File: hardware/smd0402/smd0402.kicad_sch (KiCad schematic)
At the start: 33 parts, among them J1 Conn_01x04, J2 Conn_01x03, U1 WCH CH32V003F4U6

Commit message: tweak toward JLC assembly files
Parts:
- C1, D1, R1: JLC (none) -> 0402

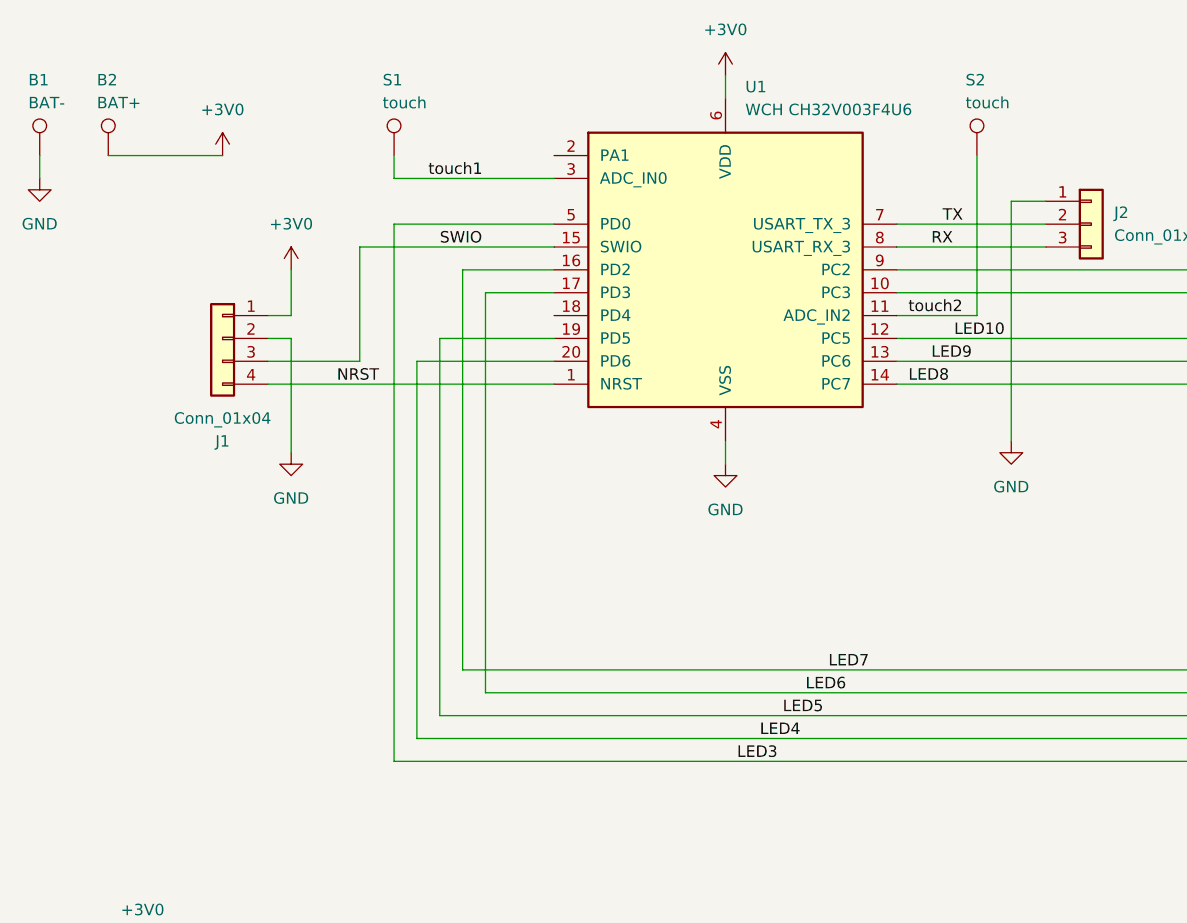
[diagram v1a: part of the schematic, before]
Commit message: reassign touch pads to OPNx
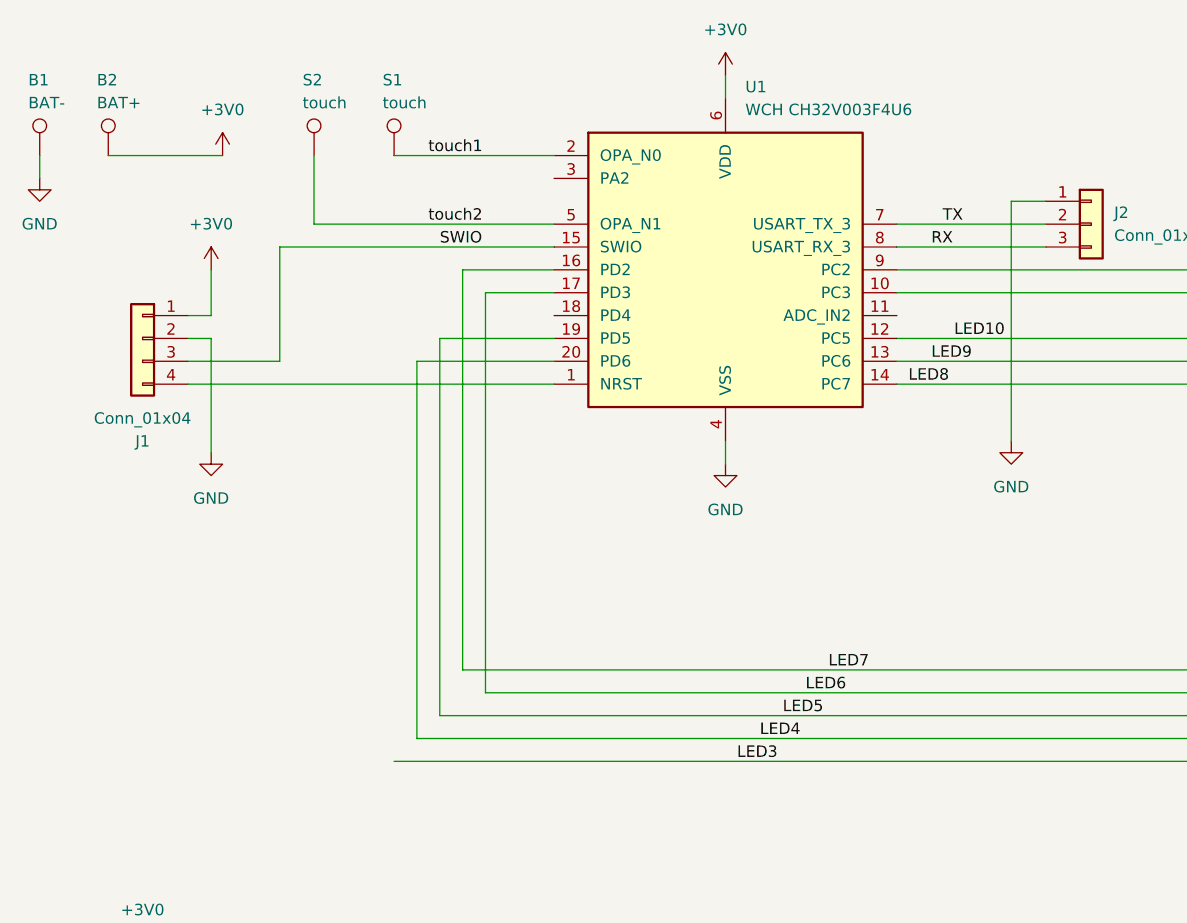
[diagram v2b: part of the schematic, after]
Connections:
- net LED3: no longer U1.5 (PD0)
- net touch1: now also U1.2 (PA1); no longer U1.3 (PA2)
- net touch2: now also U1.5 (PD0); no longer U1.11 (PC4)
- net NRST: no longer names the net of J1.4 (Pin_4), U1.1 (PD7)
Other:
- moved on the sheet: J1, S2
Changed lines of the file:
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@@
 	(wire
 		(pts
+			(xy 88.9 57.15) (xy 62.23 57.15)
+		)
+		(stroke
+			(width 0)
+			(type default)
+		)
+	)
+	(wire
+		(pts
 			(xy 176.53 62.23) (xy 127 62.23)
 		)
@@
 	(wire
 		(pts
-			(xy 57.15 69.85) (xy 59.69 69.85)
+			(xy 48.26 69.85) (xy 50.8 69.85)
 		)
 		(stroke
@@
 	(wire
 		(pts
-			(xy 67.31 59.69) (xy 88.9 59.69)
+			(xy 58.42 59.69) (xy 88.9 59.69)
 		)
 		(stroke
@@
 	(wire
 		(pts
-			(xy 59.69 67.31) (xy 57.15 67.31)
+			(xy 50.8 67.31) (xy 48.26 67.31)
 		)
 		(stroke
@@
 	(wire
 		(pts
-			(xy 57.15 74.93) (xy 88.9 74.93)
-		)
-		(stroke
-			(width 0)
-			(type default)
-		)
-	)
-	(wire
-		(pts
-			(xy 71.12 57.15) (xy 71.12 116.84)
-		)
-		(stroke
-			(width 0)
-			(type default)
-		)
-	)
-	(wire
-		(pts
 			(xy 217.17 161.29) (xy 228.6 161.29)
 		)
@@
 	(wire
 		(pts
-			(xy 71.12 52.07) (xy 71.12 49.53)
-		)
-		(stroke
-			(width 0)
-			(type default)
-		)
-	)
-	(wire
-		(pts
 			(xy 166.37 158.75) (xy 166.37 161.29)
 		)
@@
 	(wire
 		(pts
-			(xy 135.89 67.31) (xy 127 67.31)
+			(xy 107.95 149.86) (xy 121.92 149.86)
 		)
 		(stroke
@@
 	(wire
 		(pts
-			(xy 107.95 149.86) (xy 121.92 149.86)
+			(xy 238.76 148.59) (xy 238.76 151.13)
 		)
 		(stroke
@@
 	(wire
 		(pts
-			(xy 238.76 148.59) (xy 238.76 151.13)
+			(xy 62.23 57.15) (xy 62.23 49.53)
 		)
 		(stroke
@@
 	(wire
 		(pts
-			(xy 71.12 57.15) (xy 88.9 57.15)
+			(xy 52.07 149.86) (xy 67.31 149.86)
 		)
 		(stroke
@@
 	(wire
 		(pts
-			(xy 52.07 149.86) (xy 67.31 149.86)
+			(xy 31.75 49.53) (xy 31.75 52.07)
 		)
 		(stroke
@@
 	(wire
 		(pts
-			(xy 31.75 49.53) (xy 31.75 52.07)
+			(xy 88.9 49.53) (xy 71.12 49.53)
 		)
 		(stroke
@@
 	(wire
 		(pts
-			(xy 88.9 52.07) (xy 71.12 52.07)
+			(xy 166.37 140.97) (xy 166.37 64.77)
 		)
 		(stroke
@@
 	(wire
 		(pts
-			(xy 166.37 140.97) (xy 166.37 64.77)
+			(xy 43.18 138.43) (xy 43.18 142.24)
 		)
 		(stroke
@@
 	(wire
 		(pts
-			(xy 43.18 138.43) (xy 43.18 142.24)
+			(xy 50.8 62.23) (xy 50.8 67.31)
 		)
 		(stroke
@@
 	(wire
 		(pts
-			(xy 59.69 62.23) (xy 59.69 67.31)
+			(xy 48.26 74.93) (xy 88.9 74.93)
 		)
 		(stroke
@@
 	(wire
 		(pts
-			(xy 67.31 72.39) (xy 57.15 72.39)
+			(xy 58.42 72.39) (xy 48.26 72.39)
 		)
 		(stroke
@@
 	(wire
 		(pts
-			(xy 135.89 49.53) (xy 135.89 67.31)
-		)
-		(stroke
-			(width 0)
-			(type default)
-		)
-	)
-	(wire
-		(pts
 			(xy 207.01 161.29) (xy 217.17 161.29)
 		)
@@
 	(wire
 		(pts
-			(xy 59.69 69.85) (xy 59.69 82.55)
+			(xy 50.8 69.85) (xy 50.8 82.55)
 		)
 		(stroke
@@
 	(wire
 		(pts
-			(xy 67.31 59.69) (xy 67.31 72.39)
+			(xy 58.42 59.69) (xy 58.42 72.39)
 		)
 		(stroke
@@
 	(label "LED10"
 		(at 133.35 69.85 0)
-		(fields_autoplaced yes)
 		(effects
 			(font
@@
 	(label "LED4"
 		(at 111.76 114.3 0)
-		(fields_autoplaced yes)
 		(effects
 			(font
@@
 	(label "TX"
 		(at 132.08 57.15 0)
-		(fields_autoplaced yes)
 		(effects
 			(font
@@
 	(label "LED8"
 		(at 128.27 74.93 0)
-		(fields_autoplaced yes)
 		(effects
 			(font
@@
 	(label "LED9"
 		(at 130.81 72.39 0)
-		(fields_autoplaced yes)
 		(effects
 			(font
@@
 	(label "LED2"
 		(at 163.83 62.23 0)
-		(fields_autoplaced yes)
 		(effects
 			(font
@@
 	(label "LED7"
 		(at 119.38 106.68 0)
-		(fields_autoplaced yes)
-		(effects
-			(font
-				(size 1.27 1.27)
-			)
-			(justify left bottom)
-		)
-	)
-	(label "NRST"
-		(at 64.77 74.93 0)
-		(fields_autoplaced yes)
 		(effects
 			(font
@@
 	)
 	(label "touch1"
-		(at 74.93 52.07 0)
-		(fields_autoplaced yes)
+		(at 74.93 49.53 0)
 		(effects
 			(font
@@
 	)
 	(label "touch2"
-		(at 128.27 67.31 0)
-		(fields_autoplaced yes)
+		(at 74.93 57.15 0)
 		(effects
 			(font
@@
 	(label "LED1"
 		(at 161.29 64.77 0)
-		(fields_autoplaced yes)
 		(effects
 			(font
@@
 	(label "LED5"
 		(at 114.3 111.76 0)
-		(fields_autoplaced yes)
 		(effects
 			(font
@@
 	(label "SWIO"
 		(at 76.2 59.69 0)
-		(fields_autoplaced yes)
 		(effects
 			(font
@@
 	(label "RX"
 		(at 130.81 59.69 0)
-		(fields_autoplaced yes)
 		(effects
 			(font
@@
 	(label "LED3"
 		(at 109.22 116.84 0)
-		(fields_autoplaced yes)
 		(effects
 			(font
@@
 	(label "LED6"
 		(at 116.84 109.22 0)
-		(fields_autoplaced yes)
 		(effects
 			(font
@@
 	(symbol
 		(lib_id "Connector_Generic:Conn_01x04")
-		(at 52.07 69.85 0)
+		(at 43.18 69.85 0)
 		(mirror y)
 		(unit 1)
@@
 		(dnp no)
 		(property "Reference" "J1"
-			(at 52.07 81.28 0)
+			(at 43.18 81.28 0)
 			(effects
 				(font
@@
 		)
 		(property "Value" "Conn_01x04"
-			(at 52.07 78.74 0)
+			(at 43.18 78.74 0)
 			(effects
 				(font
@@
 		)
 		(property "Footprint" "Connector_PinHeader_1.27mm:PinHeader_1x04_P1.27mm_Vertical"
-			(at 52.07 69.85 0)
+			(at 43.18 69.85 0)
 			(effects
 				(font
@@
 		)
 		(property "Datasheet" "~"
-			(at 52.07 69.85 0)
+			(at 43.18 69.85 0)
 			(effects
 				(font
@@
 		)
 		(property "Description" "Generic connector, single row, 01x04, script generated (kicad-library-utils/schlib/autogen/connector/)"
-			(at 52.07 69.85 0)
+			(at 43.18 69.85 0)
 			(effects
 				(font
@@
 		)
 		(property "JLC" ""
-			(at 52.07 69.85 0)
+			(at 43.18 69.85 0)
 			(effects
 				(font
@@
 	(symbol
 		(lib_id "power:+3V0")
-		(at 59.69 62.23 0)
+		(at 50.8 62.23 0)
 		(unit 1)
 		(exclude_from_sim no)
@@
 		(fields_autoplaced yes)
 		(property "Reference" "#PWR06"
-			(at 59.69 66.04 0)
+			(at 50.8 66.04 0)
 			(effects
 				(font
@@
 		)
 		(property "Value" "+3V0"
-			(at 59.69 57.15 0)
+			(at 50.8 57.15 0)
 			(effects
 				(font
@@
 		)
 		(property "Footprint" ""
-			(at 59.69 62.23 0)
+			(at 50.8 62.23 0)
 			(effects
 				(font
@@
 		)
 		(property "Datasheet" ""
-			(at 59.69 62.23 0)
+			(at 50.8 62.23 0)
 			(effects
 				(font
@@
 		)
 		(property "Description" "Power symbol creates a global label with name \"+3V0\""
-			(at 59.69 62.23 0)
+			(at 50.8 62.23 0)
 			(effects
 				(font
@@
 	(symbol
 		(lib_id "power:GND")
-		(at 59.69 82.55 0)
+		(at 50.8 82.55 0)
 		(unit 1)
 		(exclude_from_sim no)
@@
 		(fields_autoplaced yes)
 		(property "Reference" "#PWR07"
-			(at 59.69 88.9 0)
+			(at 50.8 88.9 0)
 			(effects
 				(font
@@
 		)
 		(property "Value" "GND"
-			(at 59.69 87.63 0)
+			(at 50.8 87.63 0)
 			(effects
 				(font
@@
 		)
 		(property "Footprint" ""
-			(at 59.69 82.55 0)
+			(at 50.8 82.55 0)
 			(effects
 				(font
@@
 		)
 		(property "Datasheet" ""
-			(at 59.69 82.55 0)
+			(at 50.8 82.55 0)
 			(effects
 				(font
@@
 		)
 		(property "Description" "Power symbol creates a global label with name \"GND\" , ground"
-			(at 59.69 82.55 0)
+			(at 50.8 82.55 0)
 			(effects
 				(font
@@
 	(symbol
 		(lib_id "Connector:TestPoint")
-		(at 135.89 49.53 0)
+		(at 62.23 49.53 0)
 		(unit 1)
 		(exclude_from_sim no)
@@
 		(dnp no)
 		(property "Reference" "S2"
-			(at 134.62 41.148 0)
+			(at 60.96 41.148 0)
 			(effects
 				(font
@@
 		)
 		(property "Value" "touch"
-			(at 134.62 43.688 0)
+			(at 60.96 43.688 0)
 			(effects
 				(font
@@
 		)
 		(property "Footprint" "TestPoint:TestPoint_Pad_D4.0mm"
-			(at 140.97 49.53 0)
+			(at 67.31 49.53 0)
 			(effects
 				(font
@@
 		)
 		(property "Datasheet" "~"
-			(at 140.97 49.53 0)
+			(at 67.31 49.53 0)
 			(effects
 				(font
@@
 		)
 		(property "Description" "test point"
-			(at 135.89 49.53 0)
+			(at 62.23 49.53 0)
 			(effects
 				(font
@@
 		)
 		(property "JLC" ""
-			(at 135.89 49.53 0)
+			(at 62.23 49.53 0)
 			(effects
 				(font
@@
 		)
 		(pin "5"
+			(alternate "OPA_N1")
 		)
 		(pin "8"
@@
 		)
 		(pin "2"
+			(alternate "OPA_N0")
 		)
 		(pin "3"
-			(alternate "ADC_IN0")
 		)
 		(pin "9"

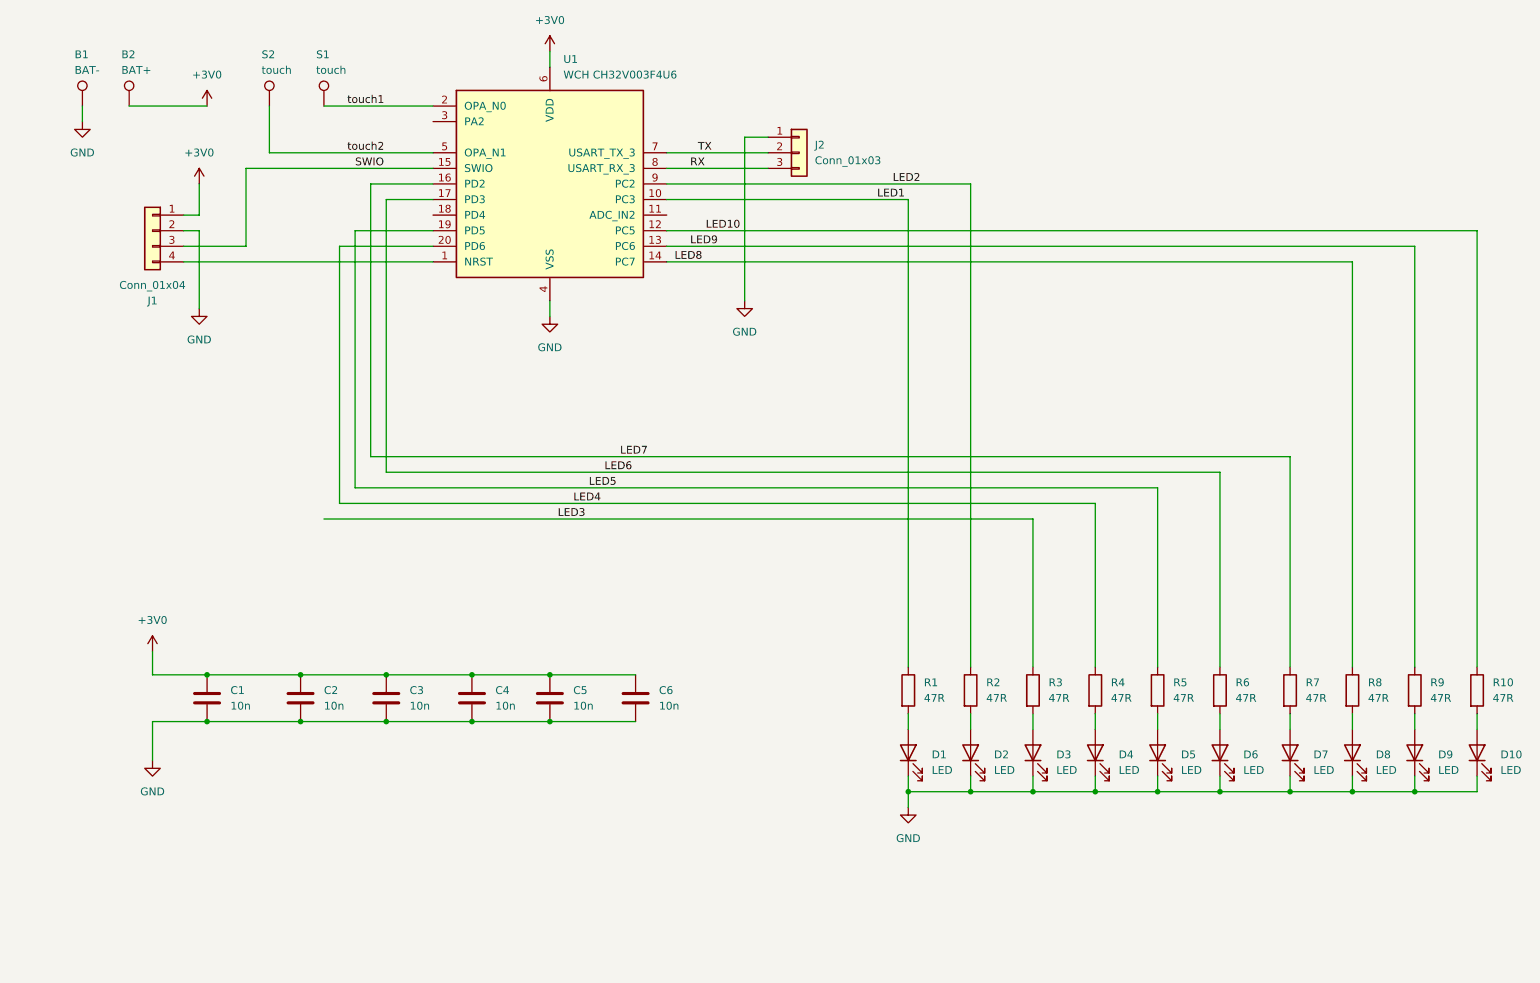
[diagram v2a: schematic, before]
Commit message: reassign pins for LEDs and touchpads
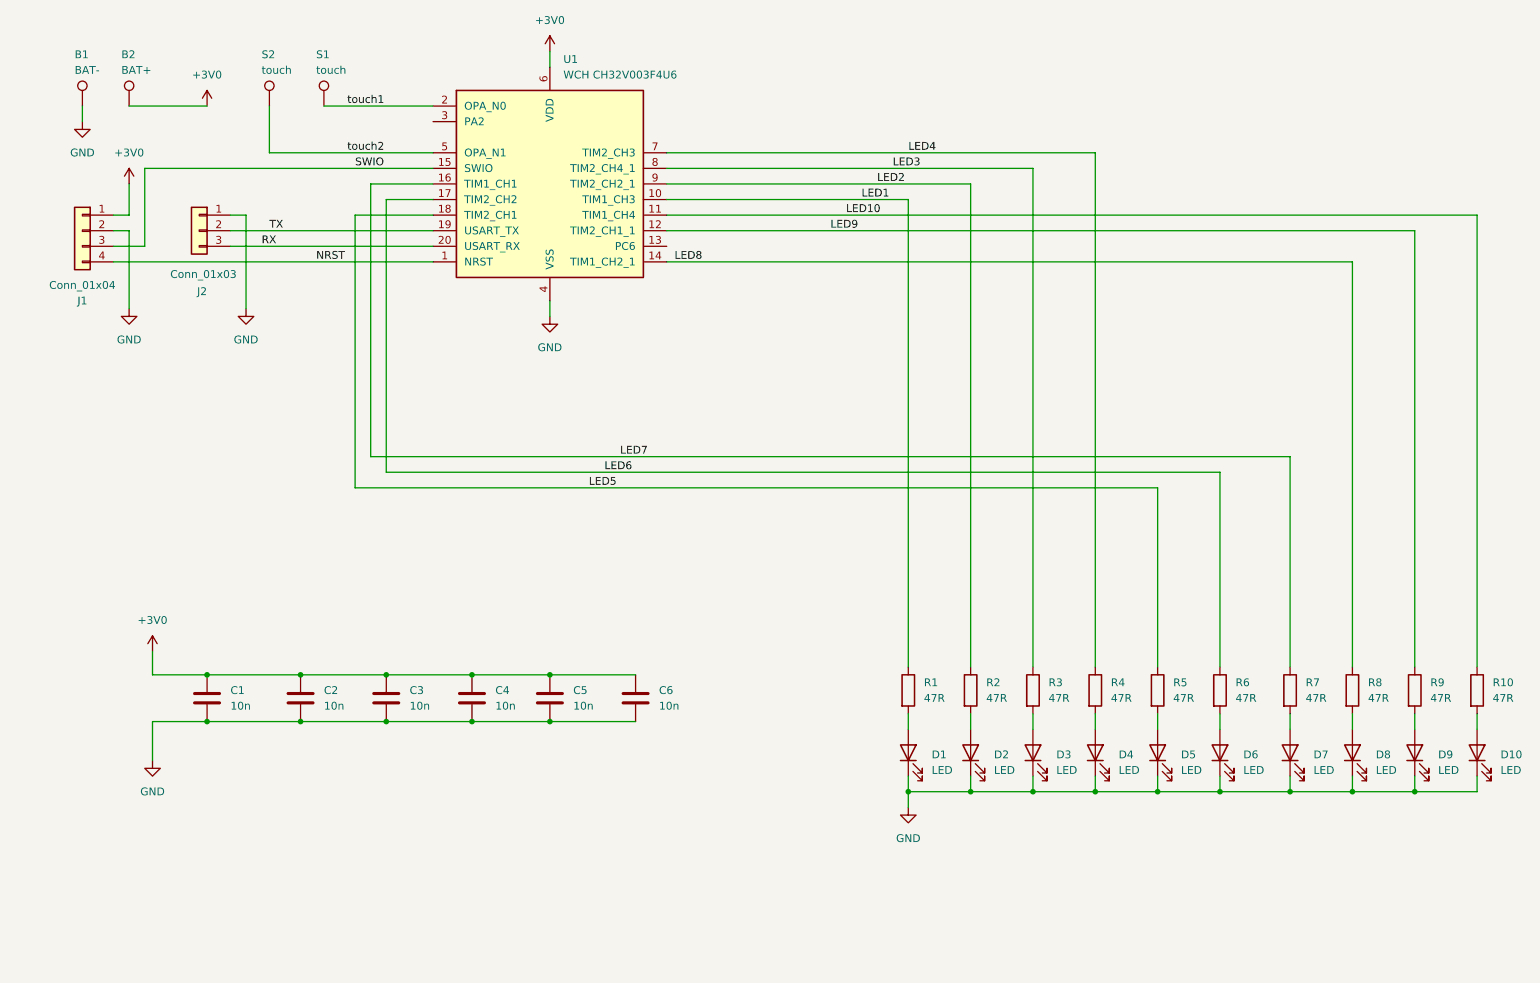
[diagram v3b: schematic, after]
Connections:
- net LED10: now also U1.11 (PC4); no longer U1.12 (PC5)
- net LED3: now also U1.8 (PC1)
- net LED4: now also U1.7 (PC0); no longer U1.20 (PD6)
- net LED5: now also U1.18 (PD4); no longer U1.19 (PD5)
- net LED9: now also U1.12 (PC5); no longer U1.13 (PC6)
- net RX: now also U1.20 (PD6); no longer U1.8 (PC1)
- net TX: now also U1.19 (PD5); no longer U1.7 (PC0)
- net NRST: now reaches J1.4 (Pin_4), U1.1 (PD7)
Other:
- moved on the sheet: J1, J2

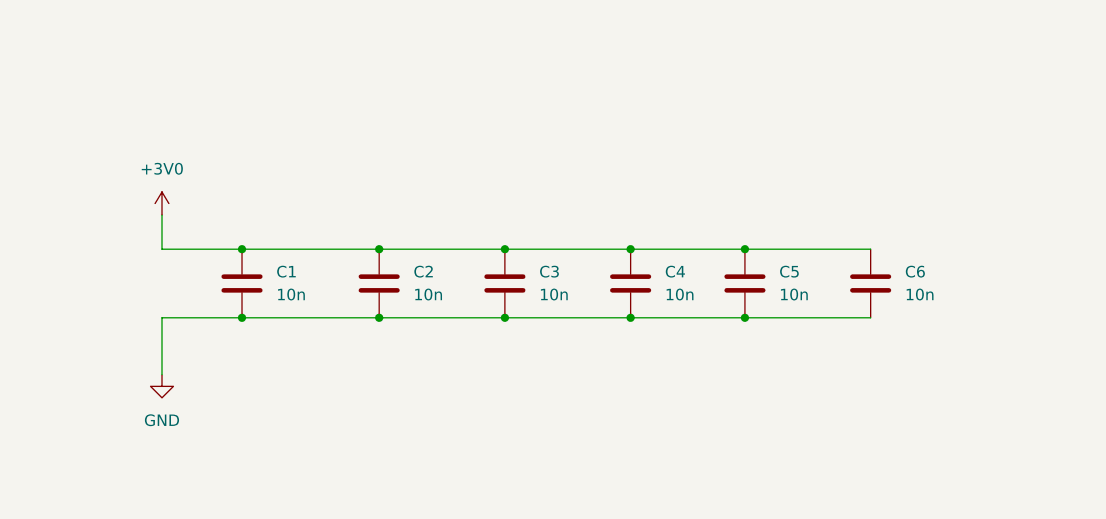
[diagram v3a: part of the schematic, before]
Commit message: change bypass caps from 10n to 1u
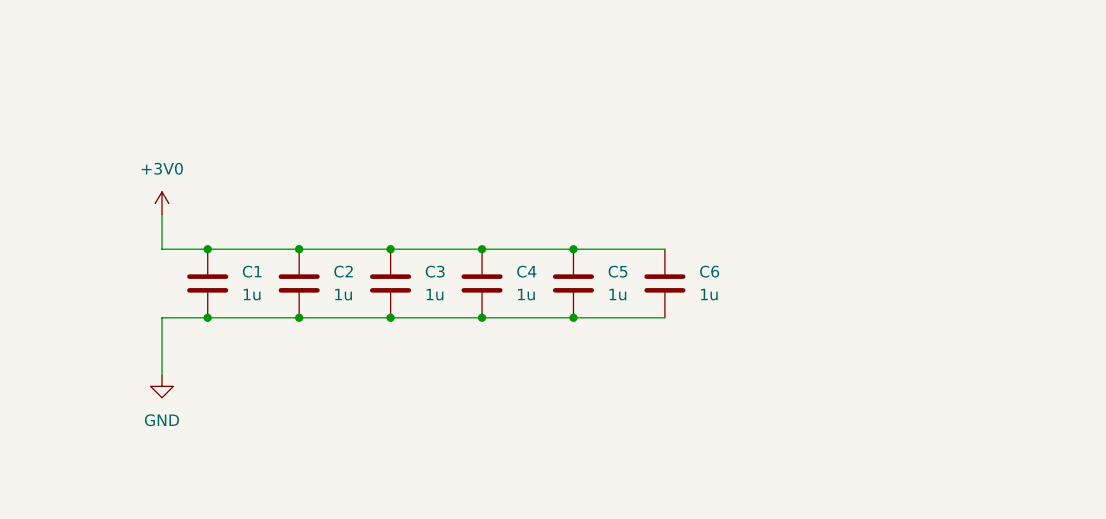
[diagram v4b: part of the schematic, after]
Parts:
- C1: value 10n -> 1u; JLC 0402 -> (none); LCSC C696856 -> C7393851
- C2, C3, C4, C5, C6: value 10n -> 1u; LCSC C696856 -> C7393851
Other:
- moved on the sheet: C6
